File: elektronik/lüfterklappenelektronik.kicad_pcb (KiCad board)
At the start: 4 copper layers, 80 x 87.6 mm, 115 parts, among them J101 Conn_01x05_Male, J102 Ckmtw_2510S-2P, J103 Conn_LAN_ENC28J60, J104 USB_B_Micro, J106 WJ2EDGRC-5.08-2P, J107 WJ2EDGRC-5.08-2P, J108 WJ2EDGRC-5.08-2P, P101 PWR_BUS_CONN1, P103 PressureSensor3, P104 PressureSensor1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

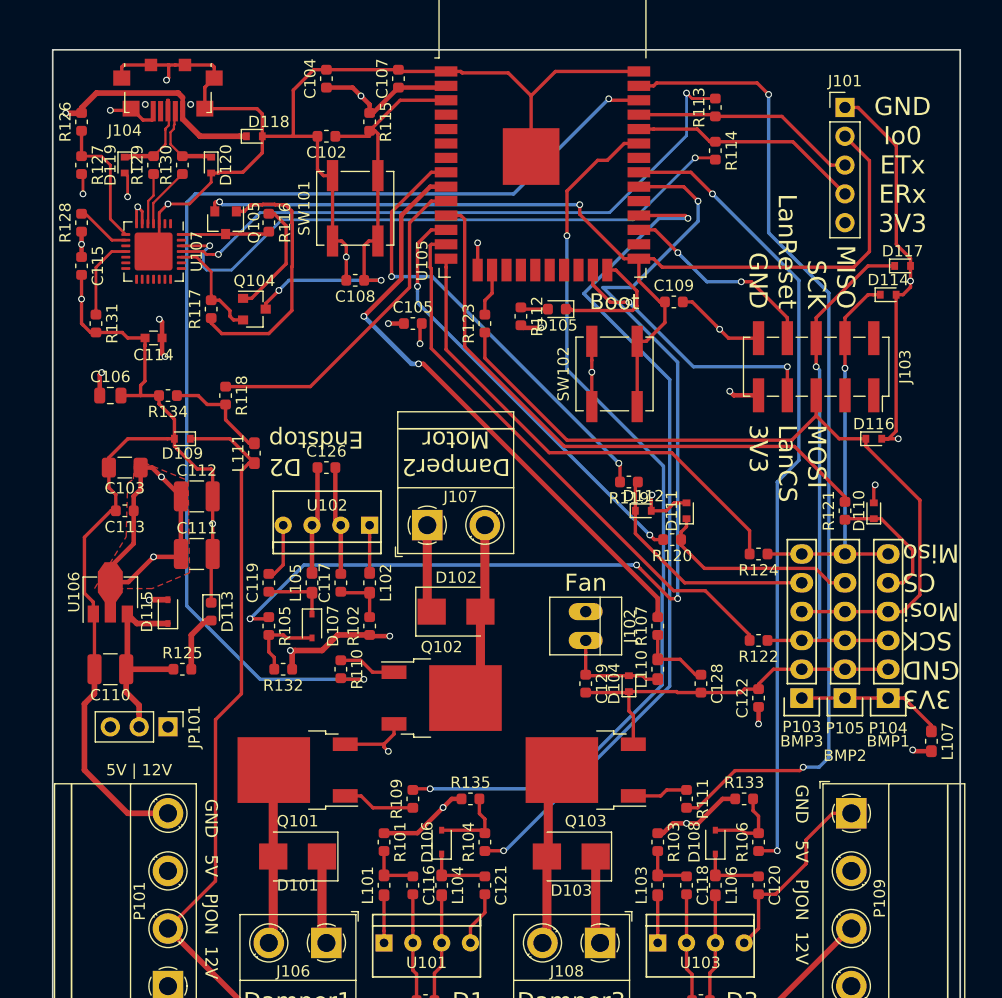
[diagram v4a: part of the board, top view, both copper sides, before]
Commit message: beautify routing, drc passed
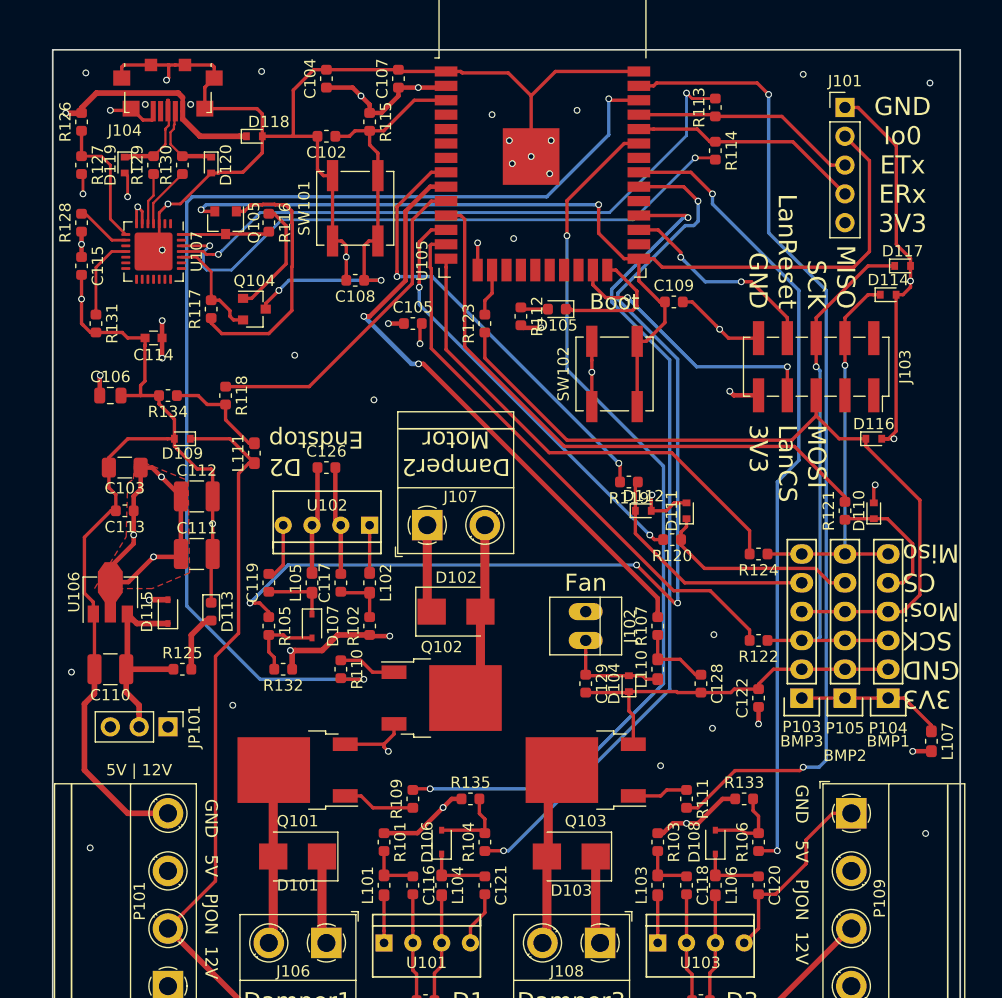
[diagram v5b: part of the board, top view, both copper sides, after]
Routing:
- net /EndstopDamper1: track 76.4 -> 73.4 mm
- net /IO0: track 88.7 -> 91.5 mm
- net /Damper2: track 99.6 -> 101.5 mm
- net /EndstopDamper2: track 91.1 -> 89.6 mm
- net GND: track 567.5 -> 566.5 mm, vias 17 -> 39
- net Net-(R119-Pad2): track 40.5 -> 39.8 mm
- net /ESP_EN: track 39.1 -> 38.5 mm
- net +3V3: track 312.7 -> 312.6 mm, vias 17 -> 19

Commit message: done
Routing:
- net /TXD: track 54.0 -> 56.4 mm
- net +3V3: track 312.6 -> 313.7 mm
- net /EndstopDamper1: track 73.4 -> 72.4 mm
- net /EndstopDamper3: track 70.8 -> 71.4 mm
- net Net-(R121-Pad2): track 52.5 -> 53.0 mm
- net /EndstopDamper2: track 89.6 -> 89.1 mm
- net GND: vias 39 -> 55
- added copper zone on F.Cu, net GND
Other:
- net class 12V: clearance 0.25 -> 0.35

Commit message: fixes. One fuckup remaining: damper2 needs different connector now
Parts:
- P103, P104, P105: footprint Pin_Headers:Pin_Header_Straight_1x06 -> Connector_PinHeader_2.54mm:PinHeader_1x06_P2.54mm_Vertical
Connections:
- J103 pad 1: (no net) -> /LAN_CLKOUT
- J103 pad 2: (no net) -> /LAN_INT
- J103 pad 3: (no net) -> /LAN_WOL
- J104 pad 4: (no net) -> Net-(J104-Pad4)
- U105 pad 17: (no net) -> Net-(U105-Pad17)
- U105 pad 18: (no net) -> Net-(U105-Pad18)
- U105 pad 19: (no net) -> Net-(U105-Pad19)
- U105 pad 20: (no net) -> Net-(U105-Pad20)
- U105 pad 21: (no net) -> Net-(U105-Pad21)
- U105 pad 22: (no net) -> Net-(U105-Pad22)
- U105 pad 26: (no net) -> /SDA
- U105 pad 29: (no net) -> /SCL
- U105 pad 32: (no net) -> Net-(U105-Pad32)
- U105 pad 4: (no net) -> Net-(U105-Pad4)
- U105 pad 5: (no net) -> Net-(U105-Pad5)
- U105 pad 6: (no net) -> Net-(U105-Pad6)
- U105 pad 7: (no net) -> Net-(U105-Pad7)
- U107 pad 1: (no net) -> /DCD
- U107 pad 10: (no net) -> Net-(U107-Pad10)
- U107 pad 12: (no net) -> Net-(U107-Pad12)
- U107 pad 13: (no net) -> Net-(U107-Pad13)
- U107 pad 14: (no net) -> Net-(U107-Pad14)
- U107 pad 15: (no net) -> Net-(U107-Pad15)
- U107 pad 16: (no net) -> Net-(U107-Pad16)
- U107 pad 17: (no net) -> Net-(U107-Pad17)
- U107 pad 18: (no net) -> Net-(U107-Pad18)
- U107 pad 19: (no net) -> Net-(U107-Pad19)
- U107 pad 2: (no net) -> /RI
- U107 pad 20: (no net) -> Net-(U107-Pad20)
- U107 pad 21: (no net) -> Net-(U107-Pad21)
- U107 pad 22: (no net) -> Net-(U107-Pad22)
- U107 pad 23: (no net) -> /CTS
- U107 pad 27: (no net) -> /DSR

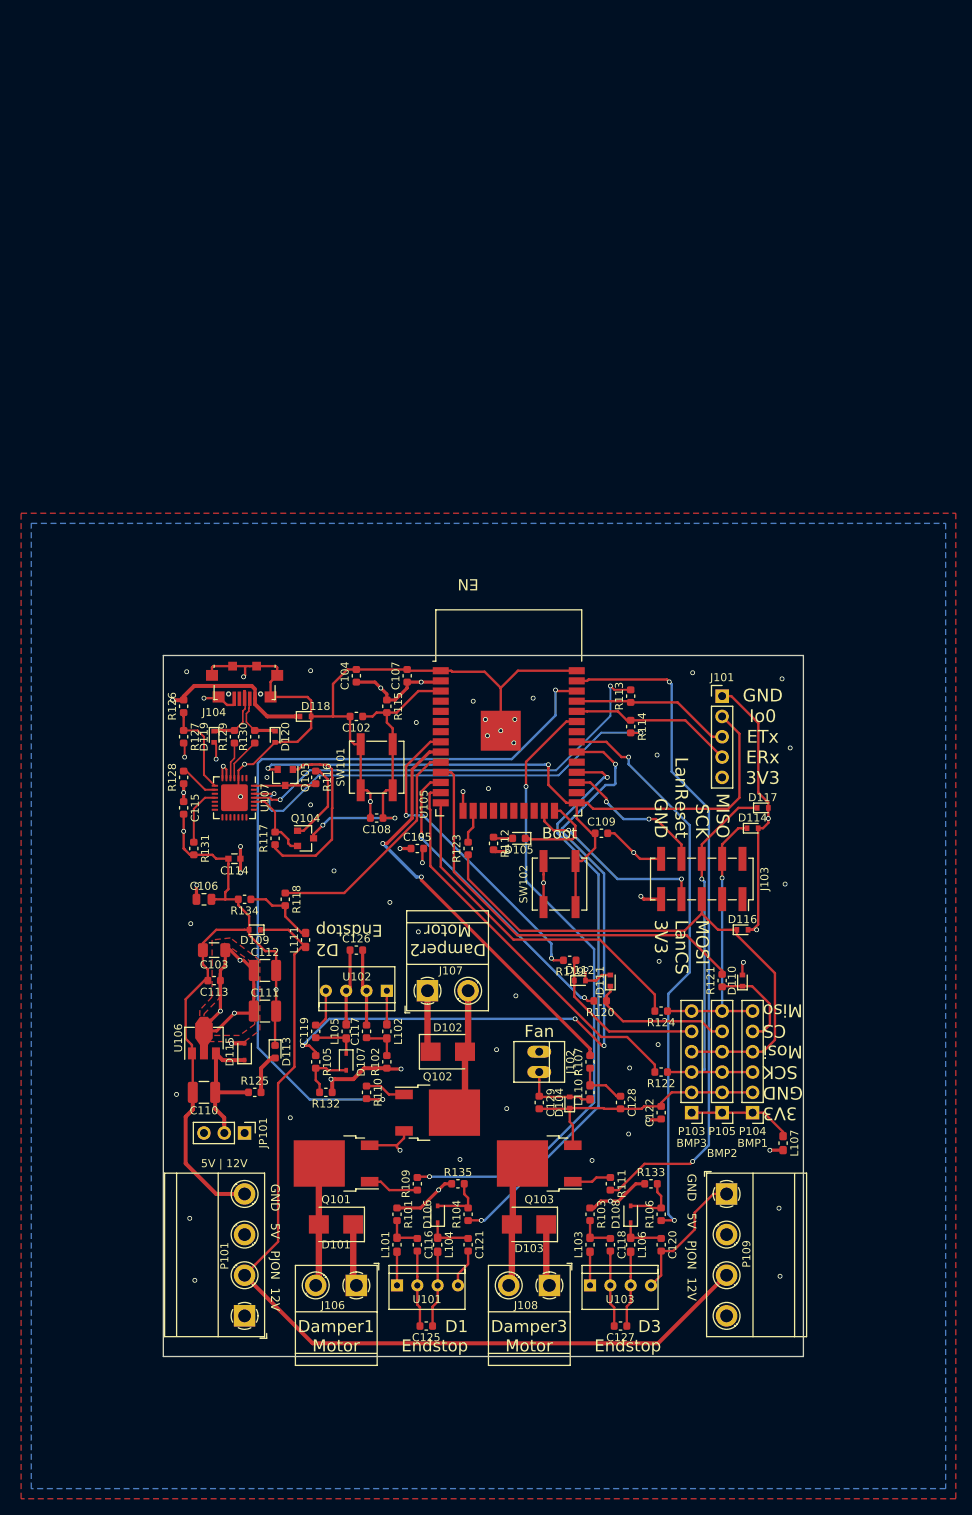
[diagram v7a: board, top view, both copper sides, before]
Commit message: change to vertical footprint and make some space for corrently sized courtyards
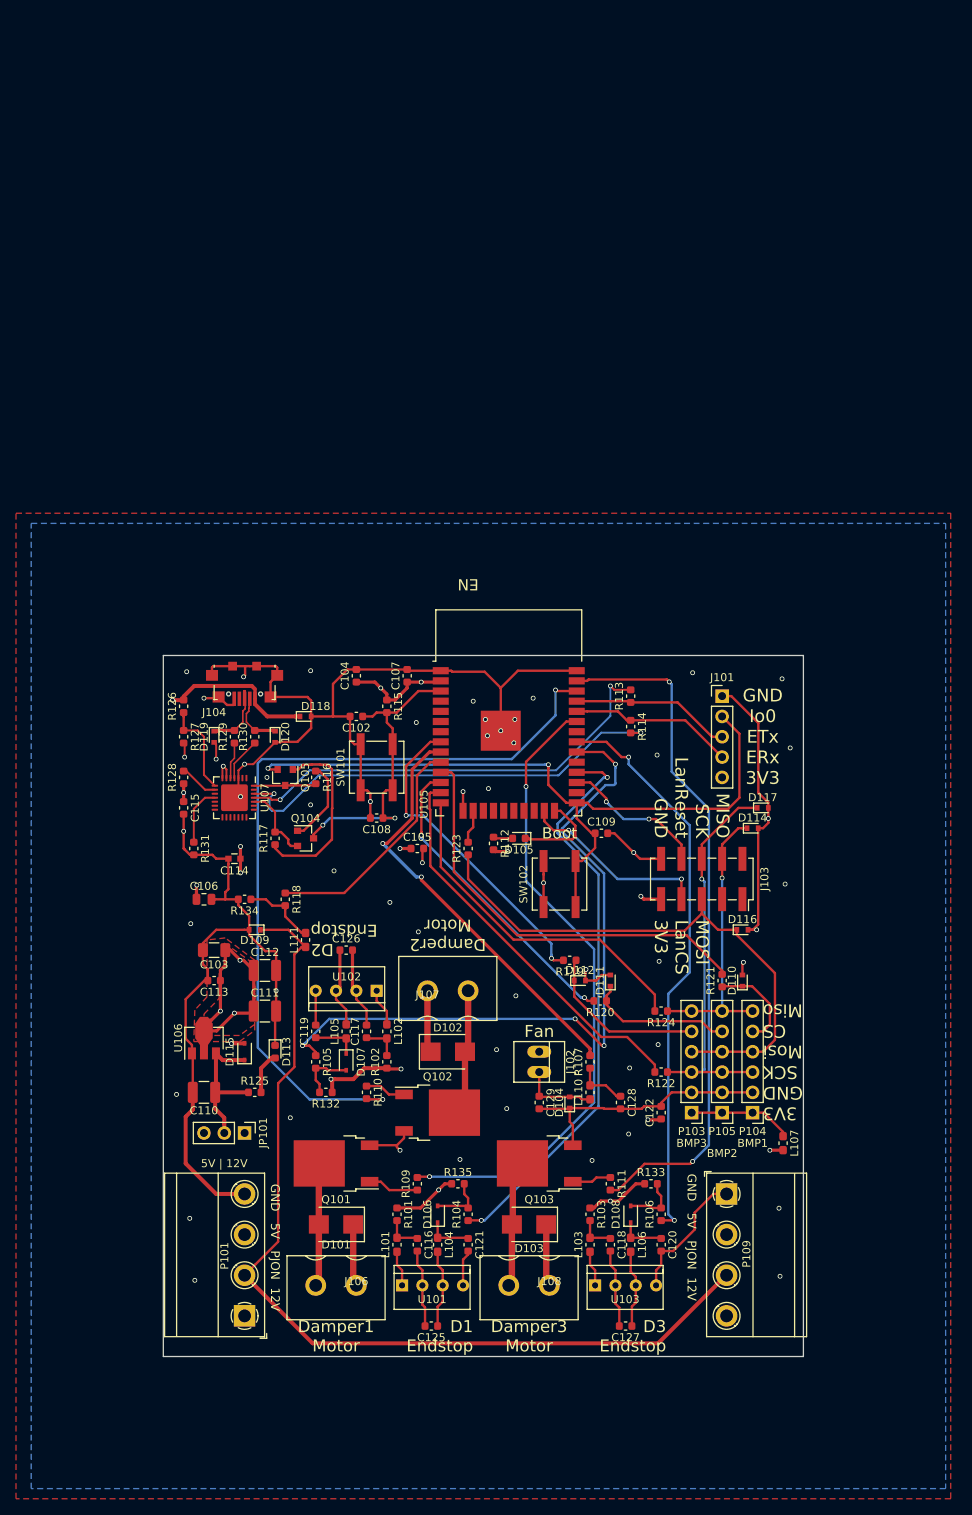
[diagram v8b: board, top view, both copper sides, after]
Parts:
- J106, J107, J108: value WJ2EDGRC-5.08-2P -> WJ2EDGVC-5.08-2P; footprint FootprintsTittelbach:WJ2EDGRC-5.08-2P -> FootprintsTittelbach:WJ2EDGVC-5.08-2P
- moved C126 1.27 mm to (85.1, 86.4)
- moved U102 1.27 mm to (88.9, 91.4)
- moved C125 0.64 mm to (95.7, 133.3)
- moved C127 0.64 mm to (120.0, 133.3)
- moved U101 0.64 mm to (92.1, 128.3)
- moved U103 0.64 mm to (116.2, 128.3)
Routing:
- net GND: track 566.5 -> 616.5 mm
- net Net-(C126-Pad1): track 9.48 -> 10.0 mm
- net Net-(L102-Pad1): track 4.20 -> 4.73 mm
